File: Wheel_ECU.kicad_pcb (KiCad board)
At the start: 2 copper layers, 61 x 61 mm, 64 parts, among them J1 Conn_01x04, J2 Conn_01x04, J3 Conn_01x02, J4 Debug, J5 Conn_01x02, U1 IFX9201SG, U2 TLE4964, U3 XMC1404_F064, U4 TLE7251, U5 LM35-D

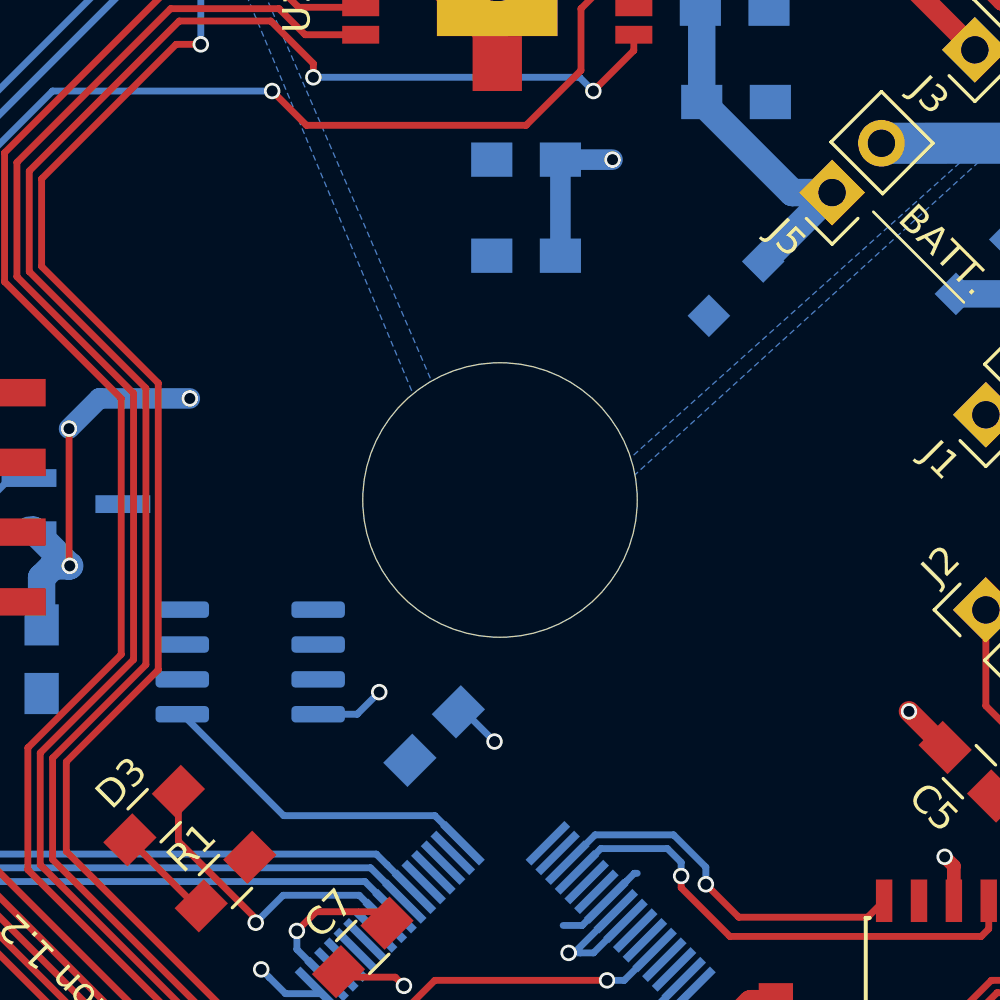
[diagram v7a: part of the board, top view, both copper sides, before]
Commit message: Join the mount holes with the motor hole
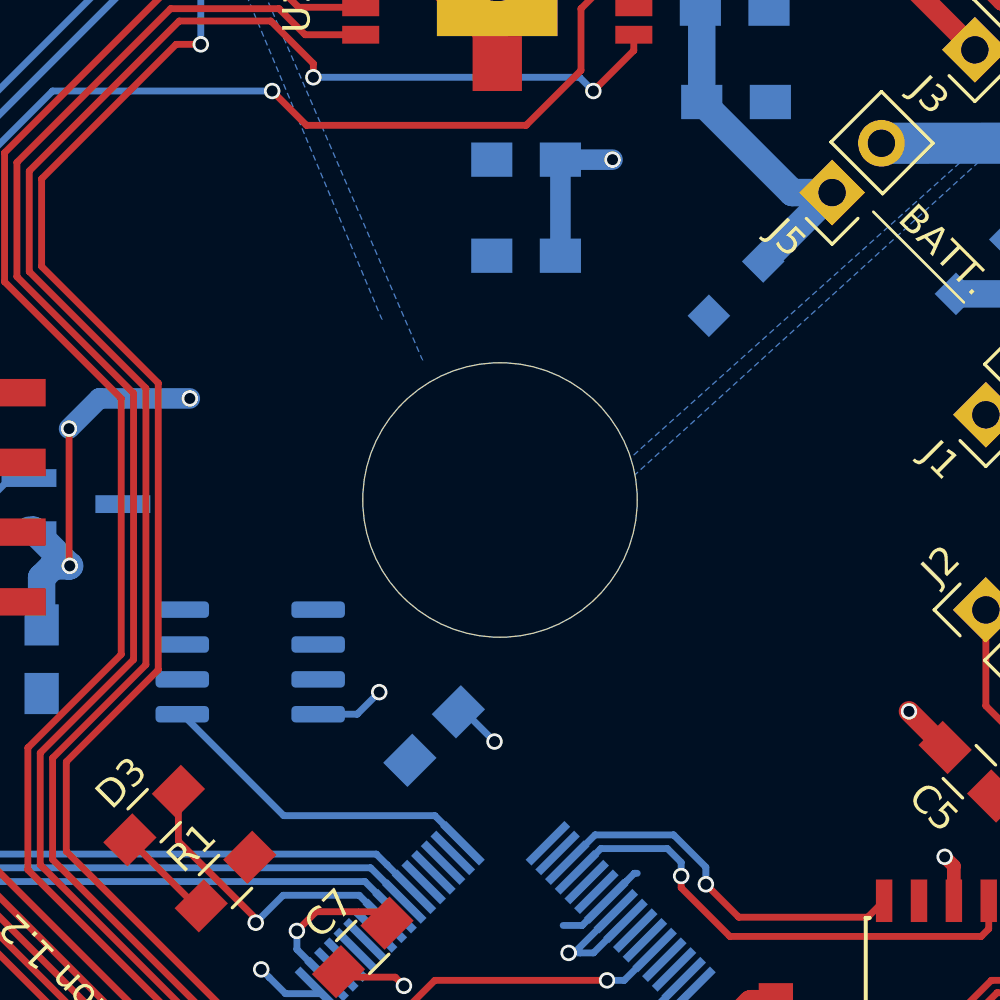
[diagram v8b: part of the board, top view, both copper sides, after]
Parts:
- removed the M** at (123.5, 90.1)
- removed the M** at (140.1, 106.7)
- added M**: Motor_Mount_Hole, WheelECU:Mount_Hole_M3x6.5, F.Cu at (125.3, 91.9)
- added M**: Motor_Mount_Hole, WheelECU:Mount_Hole_M3x6.5, F.Cu at (138.3, 104.9)
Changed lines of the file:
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@@
     (add_net CAN-)
+  )
+  (module WheelECU:Mount_Hole_M3x6.5 (layer F.Cu)
+    (at 125.275 91.875 135)
+    (fp_text reference M** (at -1.2 3.2 135) (layer F.SilkS) hide
+      (effects (font (size 1 1) (thickness 0.15)))
+    )
+    (fp_text value Motor_Mount_Hole (at 0 -3.5 135) (layer F.Fab) hide
+      (effects (font (size 1 1) (thickness 0.15)))
+    )
+    (pad "" np_thru_hole oval (at 0 0 135) (size 14.75 3.2) (drill oval 14.75 3.2) (layers *.Cu *.Mask)
+      (solder_mask_margin 1.2) (clearance 1.4))
+  )
+  (module WheelECU:Mount_Hole_M3x6.5 (layer F.Cu)
+    (at 138.325 104.925 135)
+    (fp_text reference M** (at -1.2 3.2 135) (layer F.SilkS) hide
+      (effects (font (size 1 1) (thickness 0.15)))
+    )
+    (fp_text value Motor_Mount_Hole (at 0 -3.5 135) (layer F.Fab) hide
+      (effects (font (size 1 1) (thickness 0.15)))
+    )
+    (pad "" np_thru_hole oval (at 0 0 135) (size 14.75 3.2) (drill oval 14.75 3.2) (layers *.Cu *.Mask)
+      (solder_mask_margin 1.2) (clearance 1.4))
   )
   (module WheelECU:Key_Hole_3mm (layer F.Cu)
@@
     (pad "" np_thru_hole circle (at 0 0) (size 10 10) (drill 10) (layers *.Cu *.Mask)
       (solder_mask_margin 0.01) (clearance 0.01))
-  )
-  (module WheelECU:Mount_Hole_M3x6.5 (layer F.Cu)
-    (at 123.5 90.1 135)
-    (fp_text reference M** (at -1.2 3.2 135) (layer F.SilkS) hide
-      (effects (font (size 1 1) (thickness 0.15)))
-    )
-    (fp_text value Motor_Mount_Hole (at 0 -3.5 135) (layer F.Fab) hide
-      (effects (font (size 1 1) (thickness 0.15)))
-    )
-    (pad "" np_thru_hole oval (at 0 0 135) (size 9.75 3.2) (drill oval 9.75 3.2) (layers *.Cu *.Mask)
-      (solder_mask_margin 1.2) (clearance 1.4))
   )
   (module WheelECU:Pin_Header_Straight_2x04_Pitch2.54mm_SMD (layer F.Cu)
@@
     )
   )
-  (module WheelECU:Mount_Hole_M3x6.5 (layer F.Cu)
-    (at 140.1 106.7 135)
-    (fp_text reference M** (at -1.2 3.2 135) (layer F.SilkS) hide
-      (effects (font (size 1 1) (thickness 0.15)))
-    )
-    (fp_text value Motor_Mount_Hole (at 0 -3.5 135) (layer F.Fab) hide
-      (effects (font (size 1 1) (thickness 0.15)))
-    )
-    (pad "" np_thru_hole oval (at 0 0 135) (size 9.75 3.2) (drill oval 9.75 3.2) (layers *.Cu *.Mask)
-      (solder_mask_margin 1.2) (clearance 1.4))
-  )
   (module WheelECU:TQFP-64_10x10mm_Pitch0.5mm_Handsoldering (layer B.Cu)
